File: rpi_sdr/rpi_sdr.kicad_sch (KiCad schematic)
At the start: 2 parts

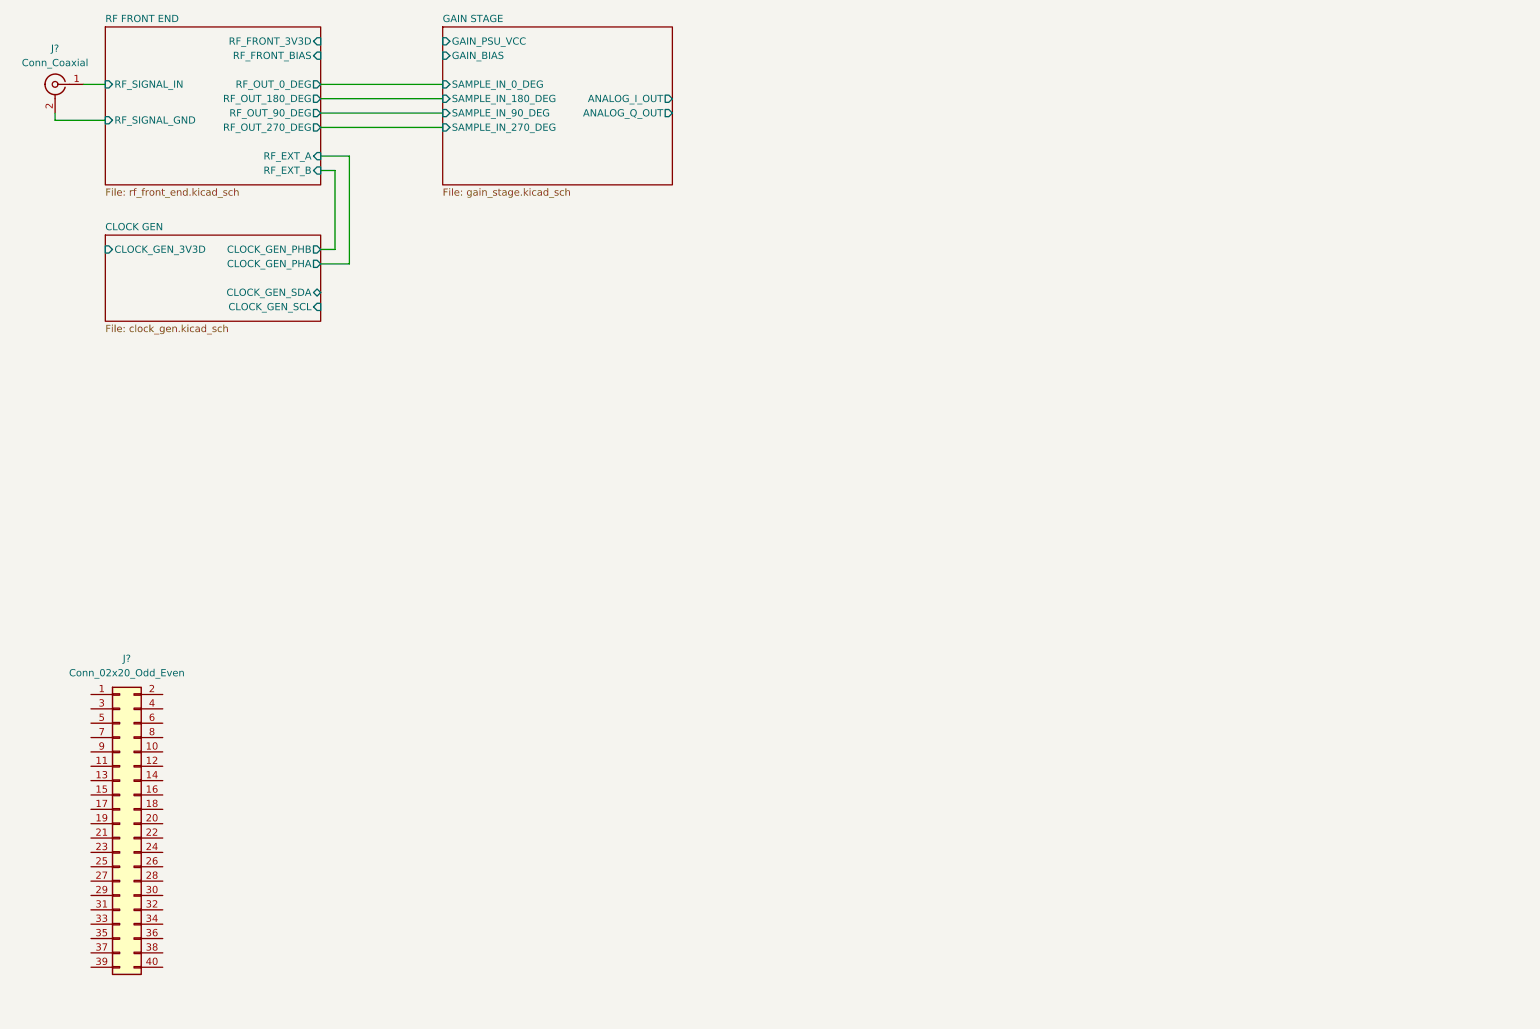
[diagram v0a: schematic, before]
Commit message: update schematic: add audio card, etc
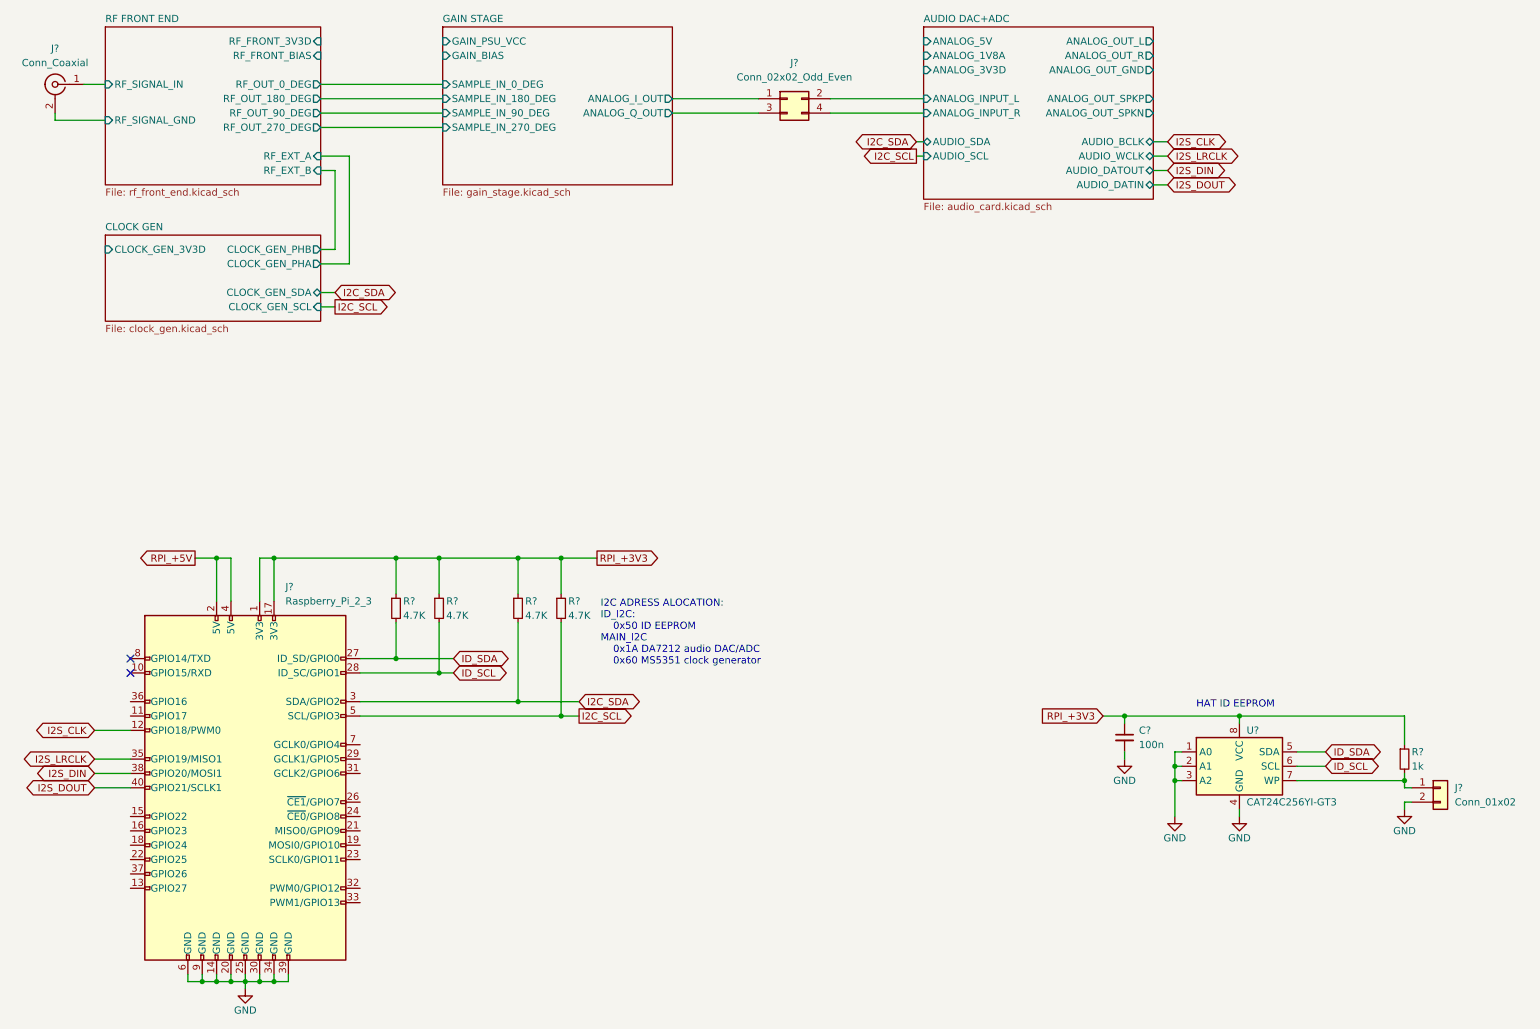
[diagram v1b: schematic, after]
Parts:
- removed J?: Conn_02x20_Odd_Even, symbol Connector_Generic:Conn_02x20_Odd_Even
- added C?: 100n, symbol Device:C_Small
- added J?: Raspberry_Pi_2_3, Connector_PinSocket_2.54mm:PinSocket_2x20_P2.54mm_Vertical, symbol Connector:Raspberry_Pi_2_3
- added J?: Conn_01x02, symbol Connector_Generic:Conn_01x02
- added J?: Conn_02x02_Odd_Even, symbol Connector_Generic:Conn_02x02_Odd_Even
- added R? (x4): 4.7K, symbol Device:R_Small
- added R?: 1k, symbol Device:R_Small
- added U?: CAT24C256YI-GT3, Package_SO:TSSOP-8_4.4x3mm_P0.65mm, symbol Memory_EEPROM:CAT24C256
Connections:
- net GAIN STAGE/ANALOG_I_OUT: now also J?.1 (Pin_1)
- net GAIN STAGE/ANALOG_Q_OUT: now also J?.3 (Pin_3)
- new net: J?.1 (Pin_1), R?.2, U?.7 (WP)
- new net AUDIO DAC+ADC/ANALOG_INPUT_L: J?.2 (Pin_2)
- new net AUDIO DAC+ADC/ANALOG_INPUT_R: J?.4 (Pin_4)
- new net GND: C?.2, J?.14 (GND), J?.2 (Pin_2), J?.20 (GND), J?.25 (GND), J?.30 (GND), J?.34 (GND), J?.39 (GND), J?.6 (GND), J?.9 (GND), U?.1 (A0), U?.2 (A1), U?.3 (A2), U?.4 (GND)
- new net I2C_SCL: J?.5 (SCL/GPIO3), R?.2
- new net I2C_SDA: J?.3 (SDA/GPIO2), R?.2
- new net I2S_CLK: J?.12 (GPIO18/PWM0)
- new net I2S_DIN: J?.38 (GPIO20/MOSI1)
- new net I2S_DOUT: J?.40 (GPIO21/SCLK1)
- new net I2S_LRCLK: J?.35 (GPIO19/MISO1)
- new net ID_SCL: J?.28 (ID_SC/GPIO1), R?.2, U?.6 (SCL)
- new net ID_SDA: J?.27 (ID_SD/GPIO0), R?.2, U?.5 (SDA)
- new net RPI_+3V3: C?.1, J?.1 (3V3), J?.17 (3V3), R?.1, R?.1, R?.1, R?.1, R?.1, U?.8 (VCC)
- new net RPI_+5V: J?.2 (5V), J?.4 (5V)
- no-connect marks 0 -> 2
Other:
- added sheet AUDIO DAC+ADC (audio_card.kicad_sch)
- note added: "HAT ID EEPROM"
- note added: "I2C ADRESS ALOCATION: ID_I2C: 0x50 ID EEPROM MAIN_I2C 0x1A DA7212 audio DAC/ADC 0x60 MS5351 clock generator"
